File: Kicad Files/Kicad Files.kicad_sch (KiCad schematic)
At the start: 0 parts

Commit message: Updating Firmware and Schematics
Upgraded the firmware code and drawn the schematics[Not complete yet, But updated].
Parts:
- added IR-1, IR-2: IR Sensor, symbol Comparator:LM393
- added M1, M2: Motor, symbol Connector_Generic:Conn_01x02
- added MotorDriver: L298N, Package_TO_SOT_THT:TO-220-15_P2.54x5.08mm_StaggerOdd_Lead4.58mm_Vertical, symbol Driver_Motor:L298N
- added SW1: SW_SPST, symbol Switch:SW_SPST
- added U1: (no value), ESP32_30pin, symbol Doit-ESP32-Devkit-v1:ESP32_30Pin
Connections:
- new net: IR-1.1, U1.12 (GPIO34)
- new net: IR-1.2 (-), IR-2.2 (-), U1.2 (GND)
- new net: M1.1 (Pin_1), MotorDriver.2 (OUT1)
- new net: M1.2 (Pin_2), MotorDriver.3 (OUT2)
- new net: M2.1 (Pin_1), MotorDriver.13 (OUT3)
- new net: M2.2 (Pin_2), MotorDriver.14 (OUT4)
- new net: MotorDriver.10 (IN3), U1.5 (GPIO14)
- new net: MotorDriver.11 (EnB), U1.7 (GPIO26)
- new net: MotorDriver.12 (IN4), U1.6 (GPIO27)
- new net: MotorDriver.5 (IN1), U1.22 (GPIO17)
- new net: MotorDriver.6 (EnA), U1.8 (GPIO25)
- new net: MotorDriver.7 (IN2), U1.21 (GPIO16)
- new net: MotorDriver.8 (GND), U1.17 (GND)
- new net: IR-2.1, U1.11 (GPIO35)
- new net: IR-2.3 (+), U1.16 (3.3v)

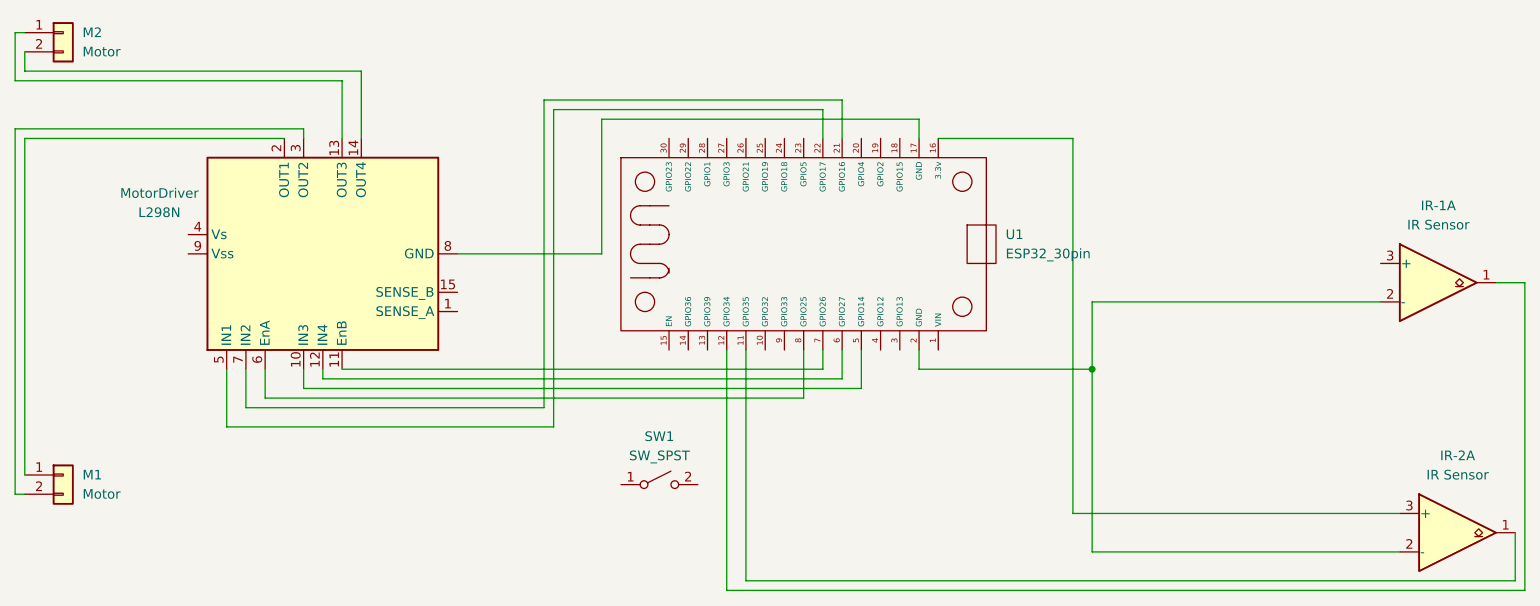
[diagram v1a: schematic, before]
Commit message: Added BOM.csv. Updated Firmware.ino,  Kicad.schematics
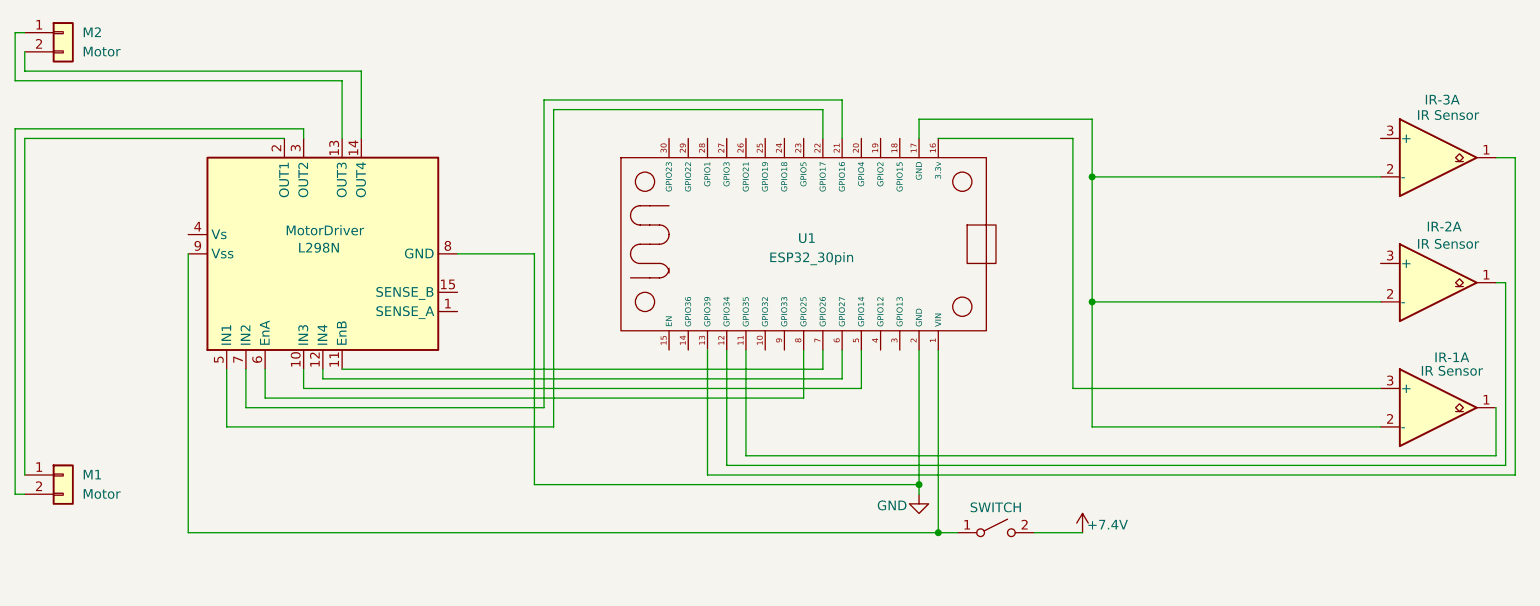
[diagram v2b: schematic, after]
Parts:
- added IR-3: IR Sensor, symbol Comparator:LM393
- SWITCH: renamed from SW1; value SW_SPST -> (none)
- renumbered IR-2 to IR-1, IR-1 to IR-2
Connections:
- net at IR-1.2 (-), IR-2.2 (-): now also U1.17 (GND), IR-3.2 (-); no longer U1.2 (GND)
- net at SWITCH.1 (A): now also MotorDriver.9 (Vss), U1.1 (VIN)
- net +7.4V: now reaches SWITCH.2 (B)
- net GND: now reaches MotorDriver.8 (GND)
- net GND: now also U1.2 (GND); no longer U1.17 (GND)
- net at U1.13 (GPIO39): now also IR-3.1
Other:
- moved on the sheet: IR-1A, SWITCH
